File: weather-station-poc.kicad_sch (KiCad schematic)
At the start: 14 parts

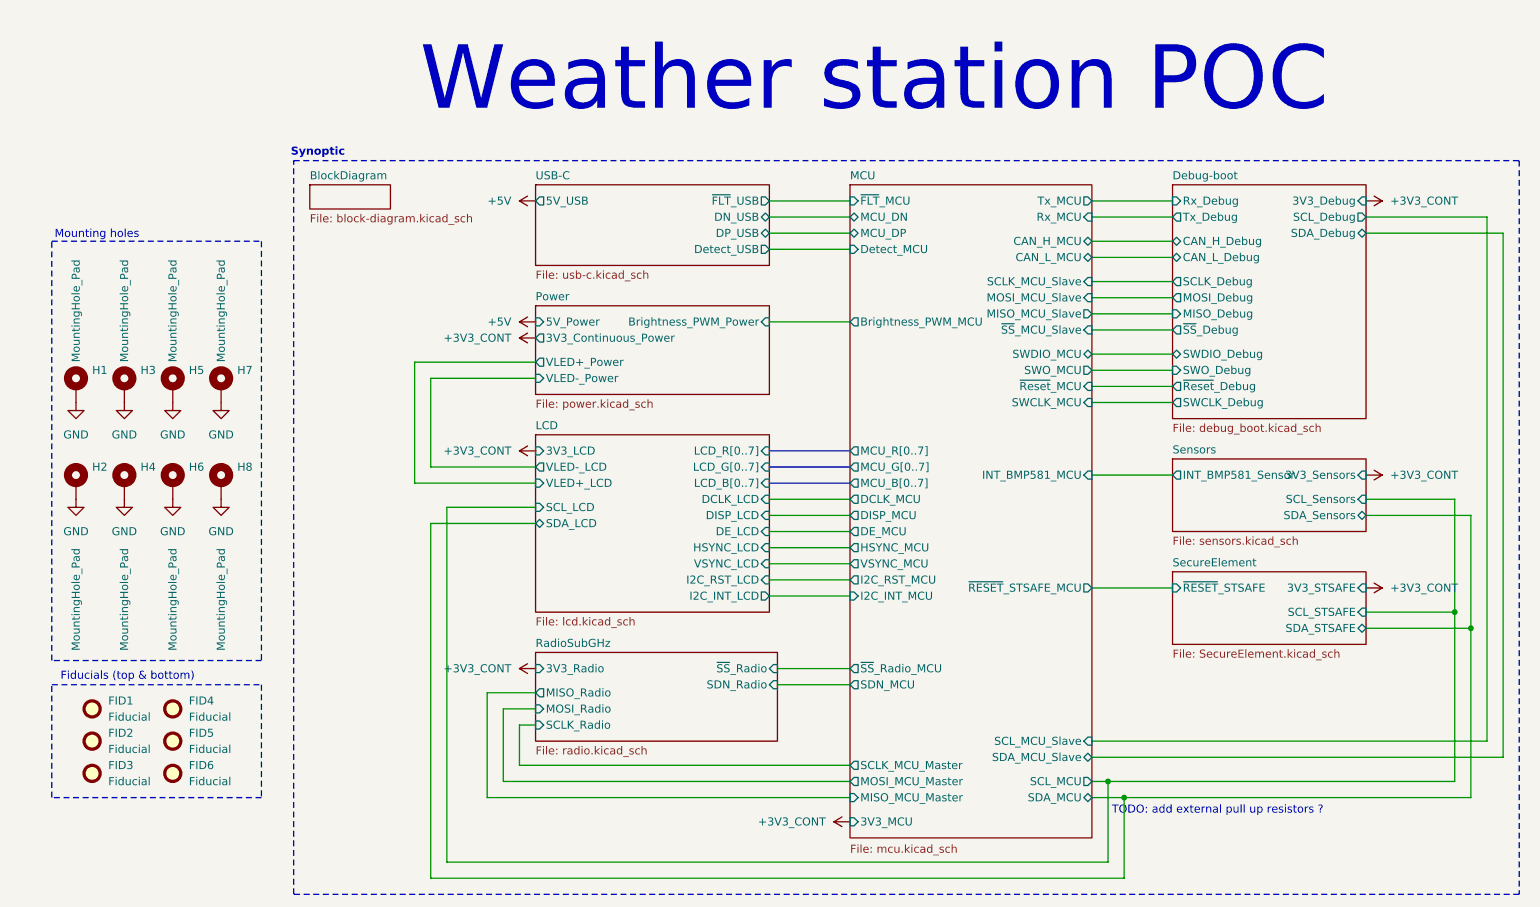
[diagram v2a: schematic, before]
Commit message: Add pull ups resistors for I2C bus and reformat some schematic files
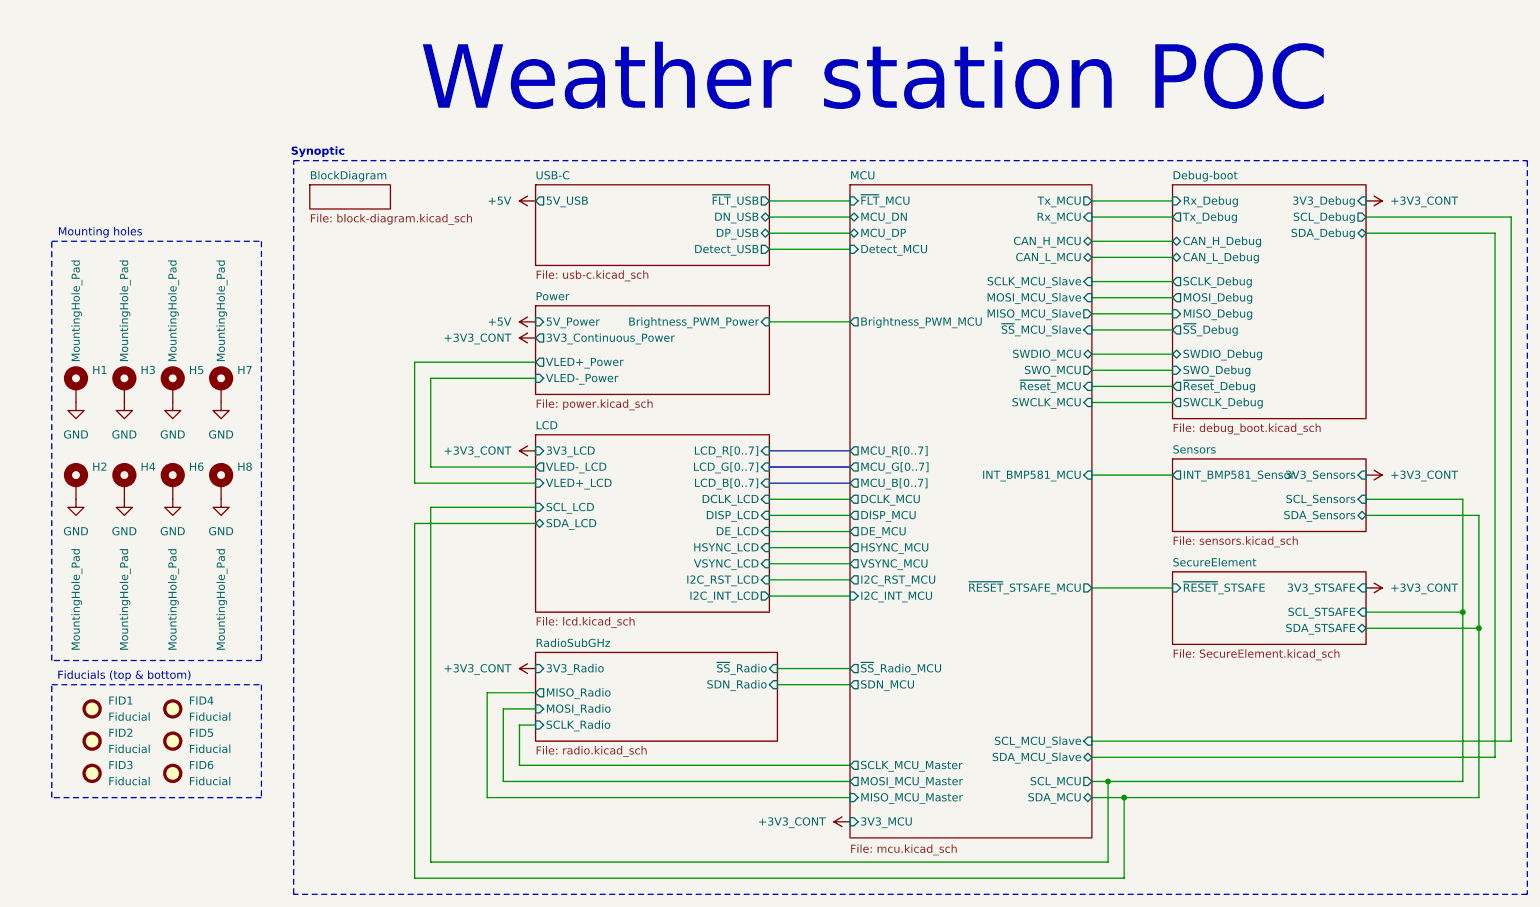
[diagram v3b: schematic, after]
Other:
- note removed: "TODO: add external pull up resistors ?"
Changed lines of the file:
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@@
 	(rectangle
 		(start 57.15 35.56)
-		(end 250.19 151.13)
+		(end 251.46 151.13)
 		(stroke
 			(width 0)
@@
 		(fill
 			(type none)
-		)
-	)
-	(text "TODO: add external pull up resistors ?"
-		(exclude_from_sim no)
-		(at 202.692 137.922 0)
-		(effects
-			(font
-				(size 1.27 1.27)
-			)
 		)
 	)
@@
 	(text "Fiducials (top & bottom)"
 		(exclude_from_sim no)
-		(at 30.988 116.84 0)
+		(at 30.48 116.84 0)
 		(effects
 			(font
@@
 	(text "Mounting holes"
 		(exclude_from_sim no)
-		(at 26.162 47.244 0)
+		(at 26.67 46.99 0)
 		(effects
 			(font
@@
 	)
 	(junction
-		(at 242.57 109.22)
-		(diameter 0)
-		(color 0 0 0 0)
-	)
-	(junction
 		(at 187.96 135.89)
 		(diameter 0)
@@
 	)
 	(junction
-		(at 240.03 106.68)
+		(at 243.84 109.22)
+		(diameter 0)
+		(color 0 0 0 0)
+	)
+	(junction
+		(at 241.3 106.68)
 		(diameter 0)
 		(color 0 0 0 0)
@@
 	(wire
 		(pts
-			(xy 226.06 106.68) (xy 240.03 106.68)
+			(xy 226.06 106.68) (xy 241.3 106.68)
 		)
 		(stroke
@@
 	(wire
 		(pts
+			(xy 78.74 90.17) (xy 95.25 90.17)
+		)
+		(stroke
+			(width 0)
+			(type default)
+		)
+	)
+	(wire
+		(pts
 			(xy 182.88 71.12) (xy 195.58 71.12)
 		)
@@
 	(wire
 		(pts
+			(xy 76.2 92.71) (xy 95.25 92.71)
+		)
+		(stroke
+			(width 0)
+			(type default)
+		)
+	)
+	(wire
+		(pts
 			(xy 87.63 119.38) (xy 87.63 135.89)
 		)
@@
 	(wire
 		(pts
-			(xy 242.57 109.22) (xy 242.57 135.89)
+			(xy 243.84 109.22) (xy 243.84 135.89)
 		)
 		(stroke
@@
 	(wire
 		(pts
-			(xy 226.06 109.22) (xy 242.57 109.22)
+			(xy 226.06 109.22) (xy 243.84 109.22)
 		)
 		(stroke
@@
 	(wire
 		(pts
+			(xy 78.74 90.17) (xy 78.74 146.05)
+		)
+		(stroke
+			(width 0)
+			(type default)
+		)
+	)
+	(wire
+		(pts
 			(xy 132.08 41.91) (xy 144.78 41.91)
 		)
@@
 	(wire
 		(pts
+			(xy 76.2 92.71) (xy 76.2 148.59)
+		)
+		(stroke
+			(width 0)
+			(type default)
+		)
+	)
+	(wire
+		(pts
 			(xy 144.78 130.81) (xy 92.71 130.81)
 		)
@@
 	(wire
 		(pts
-			(xy 78.74 92.71) (xy 95.25 92.71)
+			(xy 248.92 44.45) (xy 248.92 127)
+		)
+		(stroke
+			(width 0)
+			(type default)
+		)
+	)
+	(wire
+		(pts
+			(xy 246.38 46.99) (xy 246.38 129.54)
 		)
 		(stroke
@@
 	(wire
 		(pts
-			(xy 247.65 129.54) (xy 247.65 46.99)
-		)
-		(stroke
-			(width 0)
-			(type default)
-		)
-	)
-	(wire
-		(pts
-			(xy 226.06 88.9) (xy 240.03 88.9)
+			(xy 226.06 88.9) (xy 241.3 88.9)
 		)
 		(stroke
@@
 	(wire
 		(pts
-			(xy 182.88 129.54) (xy 247.65 129.54)
+			(xy 182.88 129.54) (xy 246.38 129.54)
 		)
 		(stroke
@@
 	(wire
 		(pts
-			(xy 245.11 127) (xy 182.88 127)
-		)
-		(stroke
-			(width 0)
-			(type default)
-		)
-	)
-	(wire
-		(pts
-			(xy 185.42 146.05) (xy 81.28 146.05)
+			(xy 182.88 127) (xy 248.92 127)
 		)
 		(stroke
@@
 	(wire
 		(pts
-			(xy 247.65 46.99) (xy 226.06 46.99)
+			(xy 226.06 46.99) (xy 246.38 46.99)
 		)
 		(stroke
@@
 	(wire
 		(pts
-			(xy 78.74 148.59) (xy 78.74 92.71)
-		)
-		(stroke
-			(width 0)
-			(type default)
-		)
-	)
-	(wire
-		(pts
-			(xy 245.11 44.45) (xy 245.11 127)
-		)
-		(stroke
-			(width 0)
-			(type default)
-		)
-	)
-	(wire
-		(pts
-			(xy 81.28 90.17) (xy 95.25 90.17)
-		)
-		(stroke
-			(width 0)
-			(type default)
-		)
-	)
-	(wire
-		(pts
 			(xy 132.08 91.44) (xy 144.78 91.44)
 		)
@@
 	(wire
 		(pts
-			(xy 226.06 44.45) (xy 245.11 44.45)
-		)
-		(stroke
-			(width 0)
-			(type default)
-		)
-	)
-	(wire
-		(pts
-			(xy 240.03 88.9) (xy 240.03 106.68)
+			(xy 226.06 44.45) (xy 248.92 44.45)
+		)
+		(stroke
+			(width 0)
+			(type default)
+		)
+	)
+	(wire
+		(pts
+			(xy 241.3 88.9) (xy 241.3 106.68)
 		)
 		(stroke
@@
 	(wire
 		(pts
-			(xy 81.28 146.05) (xy 81.28 90.17)
-		)
-		(stroke
-			(width 0)
-			(type default)
-		)
-	)
-	(wire
-		(pts
 			(xy 132.08 44.45) (xy 144.78 44.45)
 		)
@@
 	(wire
 		(pts
-			(xy 187.96 135.89) (xy 242.57 135.89)
+			(xy 76.2 148.59) (xy 187.96 148.59)
+		)
+		(stroke
+			(width 0)
+			(type default)
+		)
+	)
+	(wire
+		(pts
+			(xy 187.96 135.89) (xy 243.84 135.89)
 		)
 		(stroke
@@
 	(wire
 		(pts
-			(xy 226.06 91.44) (xy 242.57 91.44)
-		)
-		(stroke
-			(width 0)
-			(type default)
-		)
-	)
-	(wire
-		(pts
-			(xy 187.96 148.59) (xy 78.74 148.59)
+			(xy 226.06 91.44) (xy 243.84 91.44)
 		)
 		(stroke
@@
 	(wire
 		(pts
-			(xy 185.42 133.35) (xy 240.03 133.35)
-		)
-		(stroke
-			(width 0)
-			(type default)
-		)
-	)
-	(wire
-		(pts
-			(xy 240.03 106.68) (xy 240.03 133.35)
+			(xy 78.74 146.05) (xy 185.42 146.05)
+		)
+		(stroke
+			(width 0)
+			(type default)
+		)
+	)
+	(wire
+		(pts
+			(xy 185.42 133.35) (xy 241.3 133.35)
+		)
+		(stroke
+			(width 0)
+			(type default)
+		)
+	)
+	(wire
+		(pts
+			(xy 241.3 106.68) (xy 241.3 133.35)
 		)
 		(stroke
@@
 	(wire
 		(pts
-			(xy 242.57 91.44) (xy 242.57 109.22)
-		)
-		(stroke
+			(xy 243.84 91.44) (xy 243.84 109.22)
+		)
+		(stroke

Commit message: Complete all references for components
Modifgy Y1 and Y2 capacitors footprint from 0603 to 0402
Modify footprint of SWD connector
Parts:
- FID1, FID2, FID3, FID4, FID5, FID6, H1, H2, H3, H4, H5, H6, H7, H8: Manufacturer_Name (none) -> N/A; Manufacturer_Part_Number (none) -> N/A

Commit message: Rename sub-sheets for more consistency
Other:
- sheet BlockDiagram renamed block-diagram
- sheet Debug-boot renamed debug-boot
- sheet LCD renamed lcd
- sheet MCU renamed mcu
- sheet Power renamed power
- sheet RadioSubGHz renamed radio
- sheet SecureElement renamed secure-element
- sheet Sensors renamed sensors
- sheet USB-C renamed usb-c
- sheet debug-boot: file debug_boot.kicad_sch -> debug-boot.kicad_sch
- sheet secure-element: file SecureElement.kicad_sch -> secure-element.kicad_sch
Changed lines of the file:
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@@
 			(color 0 0 0 0)
 		)
-		(property "Sheetname" "Power"
+		(property "Sheetname" "power"
 			(at 95.25 57.7084 0)
 			(show_name no)
@@
 			(color 0 0 0 0)
 		)
-		(property "Sheetname" "Sensors"
+		(property "Sheetname" "sensors"
 			(at 195.58 81.8384 0)
 			(show_name no)
@@
 			(color 0 0 0 0)
 		)
-		(property "Sheetname" "RadioSubGHz"
+		(property "Sheetname" "radio"
 			(at 95.25 112.3184 0)
 			(show_name no)
@@
 			(color 0 0 0 0)
 		)
-		(property "Sheetname" "USB-C"
+		(property "Sheetname" "usb-c"
 			(at 95.25 38.6584 0)
 			(show_name no)
@@
 			(color 0 0 0 0)
 		)
-		(property "Sheetname" "MCU"
+		(property "Sheetname" "mcu"
 			(at 144.78 38.6584 0)
 			(show_name no)
@@
 			(color 0 0 0 0)
 		)
-		(property "Sheetname" "LCD"
+		(property "Sheetname" "lcd"
 			(at 95.25 78.0284 0)
 			(show_name no)
@@
 			(color 0 0 0 0)
 		)
-		(property "Sheetname" "Debug-boot"
+		(property "Sheetname" "debug-boot"
 			(at 195.58 38.6584 0)
 			(show_name no)
@@
 			)
 		)
-		(property "Sheetfile" "debug_boot.kicad_sch"
+		(property "Sheetfile" "debug-boot.kicad_sch"
 			(at 195.58 76.962 0)
 			(show_name no)
@@
 			(color 0 0 0 0)
 		)
-		(property "Sheetname" "SecureElement"
+		(property "Sheetname" "secure-element"
 			(at 195.58 99.6184 0)
 			(show_name no)
@@
 			)
 		)
-		(property "Sheetfile" "SecureElement.kicad_sch"
+		(property "Sheetfile" "secure-element.kicad_sch"
 			(at 195.58 112.522 0)
 			(show_name no)
@@
 			(color 0 0 0 0)
 		)
-		(property "Sheetname" "BlockDiagram"
+		(property "Sheetname" "block-diagram"
 			(at 59.69 38.6584 0)
 			(show_name no)
